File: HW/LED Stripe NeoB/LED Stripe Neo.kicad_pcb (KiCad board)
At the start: 2 copper layers, 109 x 13.5 mm, 22 parts, among them J1 IN-OUT, J2 IN-OUT, U1 WS2812B, U10 WS2812B, U2 WS2812B, U3 WS2812B, U4 WS2812B, U5 WS2812B, U6 WS2812B, U7 WS2812B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

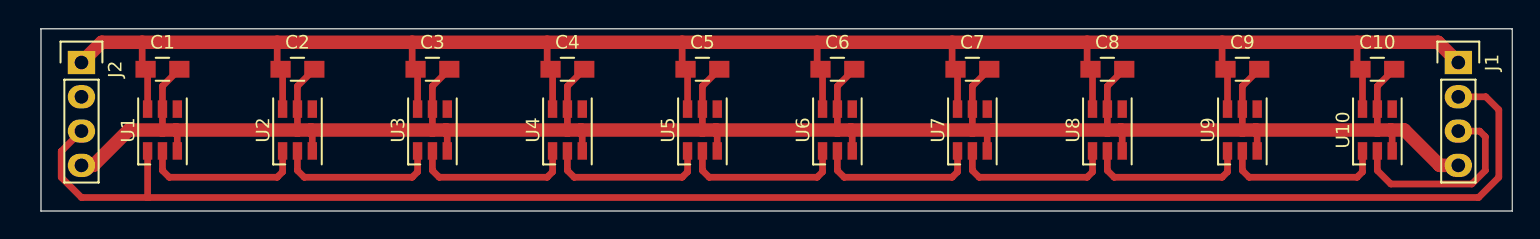
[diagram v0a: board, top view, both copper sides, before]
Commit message: WS2812B SCH/PCB added
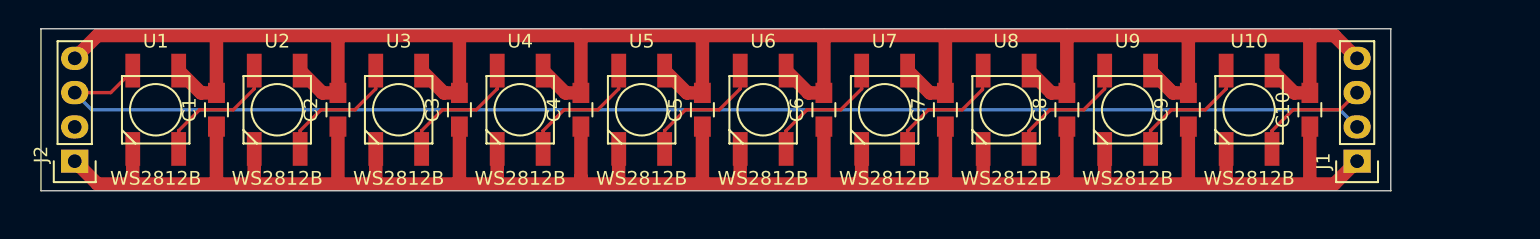
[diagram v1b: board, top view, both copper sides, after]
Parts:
- U1, U10, U2, U3, U4, U5, U6, U7, U8, U9: footprint LEDs:LED-RGB_PLLC-6 -> suf_led:LED5050-WS2812B_HANDSOLDERING
- moved J1 10.5 mm to (117.5, 29.8), turned to 180 degrees
- moved U10 9.62 mm to (109.5, 26.0), turned to 0 degrees
- moved U9 8.63 mm to (100.5, 26.0), turned to 0 degrees
- moved U8 7.65 mm to (91.5, 26.0), turned to 0 degrees
- moved J2 7.33 mm to (22.5, 29.8), turned to 180 degrees
- moved U7 6.67 mm to (82.5, 26.0), turned to 0 degrees
- moved C10 5.83 mm to (114.0, 26.0), turned to 270 degrees
- moved U6 5.70 mm to (73.5, 26.0), turned to 0 degrees
- moved C1 5.00 mm to (33.0, 26.0), turned to 270 degrees
- moved C9 5.00 mm to (105.0, 26.0), turned to 270 degrees
- moved U5 4.74 mm to (64.5, 26.0), turned to 0 degrees
- moved C2 4.24 mm to (42.0, 26.0), turned to 270 degrees
- moved C8 4.24 mm to (96.0, 26.0), turned to 270 degrees
- moved U4 3.81 mm to (55.5, 26.0), turned to 0 degrees
- moved C3 3.61 mm to (51.0, 26.0), turned to 270 degrees
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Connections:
- J2 pad 2: Net-(J2-Pad2) -> (no net)
- U1 pad 1: DO -> +5V
- U1 pad 2: Net-(U1-Pad2) -> DO
- U1 pad 3: +5V -> GND
- U1 pad 4: (no net) -> Net-(U1-Pad4)
- U10 pad 1: Net-(U10-Pad1) -> +5V
- U10 pad 2: DI -> Net-(U10-Pad2)
- U10 pad 3: +5V -> GND
- U10 pad 4: (no net) -> DI
- U2 pad 1: Net-(U1-Pad2) -> +5V
- U2 pad 2: Net-(U2-Pad2) -> Net-(U1-Pad4)
- U2 pad 3: +5V -> GND
- U2 pad 4: (no net) -> Net-(U2-Pad4)
- U3 pad 1: Net-(U2-Pad2) -> +5V
- U3 pad 2: Net-(U3-Pad2) -> Net-(U2-Pad4)
- U3 pad 3: +5V -> GND
- U3 pad 4: (no net) -> Net-(U3-Pad4)
- U4 pad 1: Net-(U3-Pad2) -> +5V
- U4 pad 2: Net-(U4-Pad2) -> Net-(U3-Pad4)
- U4 pad 3: +5V -> GND
- U4 pad 4: (no net) -> Net-(U4-Pad4)
- U5 pad 1: Net-(U4-Pad2) -> +5V
- U5 pad 2: Net-(U5-Pad2) -> Net-(U4-Pad4)
- U5 pad 3: +5V -> GND
- U5 pad 4: (no net) -> Net-(U5-Pad4)
- U6 pad 1: Net-(U5-Pad2) -> +5V
- U6 pad 2: Net-(U6-Pad2) -> Net-(U5-Pad4)
- U6 pad 3: +5V -> GND
- U6 pad 4: (no net) -> Net-(U6-Pad4)
- U7 pad 1: Net-(U6-Pad2) -> +5V
- U7 pad 2: Net-(U7-Pad2) -> Net-(U6-Pad4)
- U7 pad 3: +5V -> GND
- U7 pad 4: (no net) -> Net-(U7-Pad4)
- U8 pad 1: Net-(U7-Pad2) -> +5V
- U8 pad 2: Net-(U8-Pad2) -> Net-(U7-Pad4)
- U8 pad 3: +5V -> GND
- U8 pad 4: (no net) -> Net-(U8-Pad4)
- U9 pad 1: Net-(U8-Pad2) -> +5V
- U9 pad 2: Net-(U10-Pad1) -> Net-(U8-Pad4)
- U9 pad 3: +5V -> GND
- U9 pad 4: (no net) -> Net-(U10-Pad2)
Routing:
- net DO: track 123.7 -> 101.0 mm
- net GND: track 154.4 -> 175.2 mm
- net Net-(U8-Pad2): track 12.3 -> 0.00 mm
- net Net-(U7-Pad2): track 12.3 -> 0.00 mm
- net Net-(U6-Pad2): track 12.3 -> 0.00 mm
- net Net-(U5-Pad2): track 12.3 -> 0.00 mm
- net Net-(U4-Pad2): track 12.3 -> 0.00 mm
- net Net-(U10-Pad1): track 12.3 -> 0.00 mm
- net Net-(U3-Pad2): track 12.3 -> 0.00 mm
- net Net-(U2-Pad2): track 12.3 -> 0.00 mm
- net Net-(U1-Pad2): track 12.3 -> 0.00 mm
- net Net-(U7-Pad4): track 0.00 -> 9.58 mm
- net Net-(U1-Pad4): track 0.00 -> 9.58 mm
- net Net-(U8-Pad4): track 0.00 -> 9.58 mm
- net Net-(U6-Pad4): track 0.00 -> 9.58 mm
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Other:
- board size 109 x 13.5 mm -> 100 x 12 mm
